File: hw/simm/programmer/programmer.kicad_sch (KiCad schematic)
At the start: 10 parts, among them J101 SIMM72, SW101 SW_Push_PCB_THT, U101 74HC273, U102 RPico, U103 74HC273, U104 74HC273

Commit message: simm folder cleanup and license
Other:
- company: www.happydaze.se -> Licensed under CERN-OHL-P v2
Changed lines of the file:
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@@
     (date "2024")
     (rev "A1")
-    (company "www.happydaze.se")
+    (company "Licensed under CERN-OHL-P v2")
+    (comment 1 "Anders Granlund")
   )
   (junction (at 353.06 156.845) (diameter 0) (color 0 0 0 0)

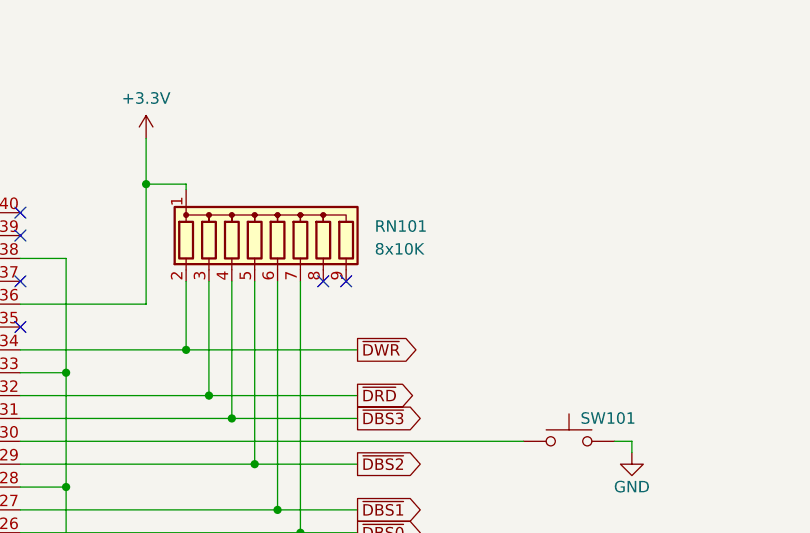
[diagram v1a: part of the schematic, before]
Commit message: corrected resistor value description, resaved with KiCad 9
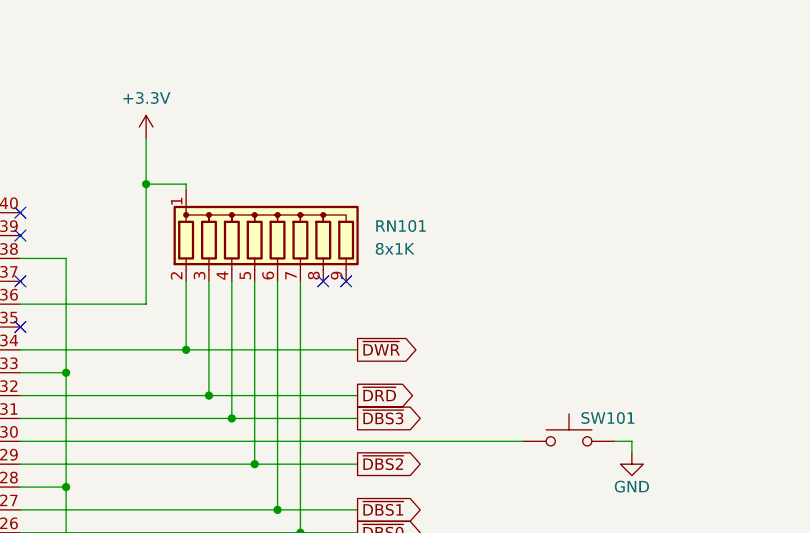
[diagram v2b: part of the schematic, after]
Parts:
- RN101: value 8x10K -> 8x1K
